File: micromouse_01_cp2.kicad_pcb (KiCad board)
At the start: 4 copper layers, 51.9 x 53 mm, 102 parts, among them IC1 ESP32-S3FH4R2, IC2 MPU-6500, IC3 AS5047P-ATSM, IC4 AS5047P-ATSM, IC5 DRV8835DSSR, IC6 PCA9632TK,118, J1 Conn_01x02, J2 USB_B_Micro, M1 MK06-4.5, M2 MK06-4.5, M3 Fan_Motor, Q1 MCM3400A-TP, Q2 MCM3400A-TP, Q3 MCM3400A-TP, Q4 SSM6J808R_LXHF, SW1 SSSS810701, SW2 SW_Push, U1 SMT-0440-S-R, U2 LBR-127HLD, U3 LBR-127HLD, U4 LBR-127HLD, U5 LBR-127HLD, U6 LXDC55FAAA-203, U7 RTV-104DF333-S-40.000-TR, U8 WS2812-2020

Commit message: エンコーダ基板シルク追加
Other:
- board text added: "L"
- board text added: "R"
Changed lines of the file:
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@@
   (gr_line (start 138 103.5) (end 132 104.000001)
     (stroke (width 0.2) (type solid)) (layer "Edge.Cuts"))
-  (gr_rect (start 118.115 79.938) (end 127.115 87.938)
+  (gr_rect locked (start 118.115 79.938) (end 127.115 87.938)
     (stroke (width 0.1) (type default)) (fill none) (layer "Edge.Cuts"))
   (gr_circle (center 162.5 102.25) (end 162.5 103.05)
@@
   (gr_circle (center 162.5 78.75) (end 162.5 79.55)
     (stroke (width 0.2) (type solid)) (fill none) (layer "Edge.Cuts"))
-  (gr_rect (start 118.68 93.26) (end 127.68 101.26)
+  (gr_rect locked (start 118.68 93.26) (end 127.68 101.26)
     (stroke (width 0.1) (type default)) (fill none) (layer "Edge.Cuts"))
+  (gr_text "L" (at 126.5 94.236191 90) (layer "B.SilkS")
+    (effects (font (size 5 5) (thickness 1) bold) (justify left bottom mirror))
+  )
+  (gr_text "R" (at 125.935 80.438 90) (layer "B.SilkS")
+    (effects (font (size 5 5) (thickness 1) bold) (justify left bottom mirror))
+  )
   (dimension (type aligned) (layer "Dwgs.User")
     (pts (xy 115.13 93.69) (xy 114.63 93.69))

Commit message: 仮変更
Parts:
- removed C12: 22u, Capacitor_SMD:C_0603_1608Metric
- removed C20, C22, C23: 1u, Capacitor_SMD:C_0402_1005Metric
- removed C21: 10u, Capacitor_SMD:C_0603_1608Metric
- removed C24: 0.01u, Capacitor_SMD:C_0402_1005Metric
- removed C25, C26, C27, C28, C29, C30, C31, C32, C35: 0.1u, Capacitor_SMD:C_0402_1005Metric
- removed IC1: ESP32-S3FH4R2, footprints:QFN40P700X700X90-57N-D
- removed J2: USB_B_Micro, footprints:WURTH_614105150721
- removed L1: 2.0nH, Inductor_SMD:L_0402_1005Metric
- removed R20: 47k, Resistor_SMD:R_0402_1005Metric
- removed SW1: SSSS810701, footprints:SSSS810701
- added C33: 0.1u, Capacitor_SMD:C_0402_1005Metric, F.Cu at (174.4, 87.0)
- added C34: 0.1u, Capacitor_SMD:C_0402_1005Metric, F.Cu at (174.4, 89.0)
- added C36: 0.1u, Capacitor_SMD:C_0402_1005Metric, F.Cu at (174.4, 91.0)
- added C37: 22u, Capacitor_SMD:C_0603_1608Metric, F.Cu at (184.6, 95.0)
- added C38: 0.1u, Capacitor_SMD:C_0402_1005Metric, F.Cu at (174.4, 92.9)
- added C41: 1u, Capacitor_SMD:C_0402_1005Metric, F.Cu at (174.4, 94.9)
- added C9: 0.1u, Capacitor_SMD:C_0402_1005Metric, F.Cu at (174.4, 85.1)
- added D7: CCS15S40,L3F, footprints:SOD-963 CST2C_TOS, F.Cu at (207.0, 115.5)
- added J3: ~, footprints:ZX62R-B-5P_30_, F.Cu at (144.3, 110.0)
- added J3: Conn_01x02_Pin, footprints:power_SMD, F.Cu at (152.5, 104.3)
- added Q5: Q_PMOS_GSD, Package_TO_SOT_SMD:SOT-23, F.Cu at (190.8, 107.1)
- added Q6: Q_PMOS_GSD, Package_TO_SOT_SMD:SOT-23, F.Cu at (190.8, 111.6)
- added R21: 10k, Resistor_SMD:R_0402_1005Metric, F.Cu at (184.1, 97.2)
- added R27: 47k, Resistor_SMD:R_0402_1005Metric, F.Cu at (194.7, 110.2)
- added R28: 47k, Resistor_SMD:R_0402_1005Metric, F.Cu at (194.7, 112.2)
- added R29: 470, Resistor_SMD:R_0402_1005Metric, F.Cu at (194.7, 114.1)
- added R32: 20, Resistor_SMD:R_0402_1005Metric, F.Cu at (209.7, 108.8)
- added R33: 20, Resistor_SMD:R_0402_1005Metric, F.Cu at (209.7, 110.8)
- added SW3: SSSS810701, footprints:SSSS810701, F.Cu at (136.3, 105.4)
- added U9: ESP32-S3-PICO-1-N8R2, footprints:QFN56_7X7_EXP, F.Cu at (151.0, 75.0)
- C18: value 0.1u -> 4.7u
- C19: value 1u -> 4.7u
- D4: value ESD9B3.3ST5G -> LED; footprint Diode_SMD:D_SOD-923 -> LED_SMD:LED_0402_1005Metric
- D5: value ESD9B3.3ST5G -> CCS15S40,L3F; footprint Diode_SMD:D_SOD-923 -> footprints:SOD-963 CST2C_TOS
- J1: value Conn_01x02 -> Conn_01x02_Pin; footprint Connector_JST:JST_PH_B2B-PH-K_1x02_P2.00mm_Vertical -> footprints:power_SMD
- Q4: value SSM6J808R_LXHF -> Q_PMOS_GSD; footprint footprints:TSOP6F_SSM6J_TOS -> Package_TO_SOT_SMD:SOT-23
- R24: value 10k -> 47k
- U7: value RTV-104DF333-S-40.000-TR -> MCP73831-2-OT; footprint Crystal:Crystal_SMD_2016-4Pin_2.0x1.6mm -> Package_TO_SOT_SMD:SOT-23-5
- moved C19 61.1 mm to (202.7, 110.1), turned to 0 degrees
- moved J1 60.8 mm to (203.7, 101.2)
- moved C18 56.8 mm to (202.7, 108.2), turned to 0 degrees
- moved R19 47.8 mm to (182.0, 71.0), turned to 0 degrees
- moved U1 47.3 mm to (168.4, 105.2)
- moved D1 46.9 mm to (167.3, 108.7), turned to 0 degrees
- moved C17 46.6 mm to (184.9, 74.7), turned to 0 degrees
- moved R18 45.5 mm to (190.8, 93.4), turned to 0 degrees
- moved U7 44.6 mm to (198.7, 109.4), turned to 0 degrees
- moved C11 43.6 mm to (184.9, 72.7), turned to 0 degrees
- moved M3 43.5 mm to (187.8, 72.5)
- moved D2 43.0 mm to (188.0, 76.2)
- moved R24 42.4 mm to (194.7, 108.2), turned to 0 degrees
- moved D5 41.7 mm to (207.0, 113.0), turned to 0 degrees
- moved Q4 41.3 mm to (190.3, 102.5), turned to 0 degrees
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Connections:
- C14 pad 1: Net-(J2-VBUS) -> VBUS
- C18 pad 1: +3V3 -> GND
- C18 pad 2: GND -> VBUS
- C19 pad 1: +3V3 -> GND
- C19 pad 2: GND -> Net-(J1-Pin_2)
- D4 pad 1: GND -> Net-(D4-K)
- D4 pad 2: USB_D- -> VBUS
- D5 pad 1: GND -> Net-(D5-K)
- D5 pad 2: USB_D+ -> VBUS
- J1 pad 1: Net-(J1-Pin_1) -> GND
- J1 pad 2: GND -> Net-(J1-Pin_2)
- Q4 pad 1: +BATT -> Net-(D5-K)
- Q4 pad 2: +BATT -> Net-(J1-Pin_2)
- R24 pad 1: Net-(IC1-CHIP_PU) -> Net-(D5-K)
- R24 pad 2: Net-(IC1-VDD3P3_1) -> GND
- U7 pad 1: unconnected-(U7-Vc-Pad1) -> /micromouse_01-2/STAT
- U7 pad 3: Net-(IC1-XTAL_P) -> Net-(J1-Pin_2)
- U7 pad 4: +3V3 -> VBUS
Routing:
- net +3V3: track 267.2 -> 48.1 mm, vias 24 -> 15
- net GND: track 101.8 -> 39.7 mm, vias 226 -> 101
- net LED_R: track 60.3 -> 0.02 mm, vias 2 -> 0
- net LED_FR: track 54.3 -> 0.00 mm, vias 2 -> 0
- net +BATT: track 53.6 -> 14.6 mm, vias 47 -> 6
- net SENS_L: track 39.3 -> 1.82 mm, vias 1 -> 0
- net LED_SDA: track 39.3 -> 2.25 mm, vias 2 -> 0
- net SENS_FR: track 43.5 -> 7.27 mm, vias 1 -> 0
- net LED_SCL: track 37.4 -> 1.31 mm, vias 2 -> 0
- net LED_FL: track 36.4 -> 1.31 mm, vias 2 -> 0
- net SENS_R: track 39.5 -> 4.99 mm, vias 1 -> 0
- net NeoPixel: track 34.3 -> 0.00 mm, vias 2 -> 0
- net USB_D-: track 33.2 -> 0.00 mm, vias 2 -> 0
- net SENS_FL: track 35.3 -> 3.36 mm, vias 1 -> 0
- net USB_D+: track 31.4 -> 0.00 mm, vias 2 -> 0
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- removed copper zone on B.Cu, net GND
- removed copper zone on In2.Cu, net GND
- removed copper zone on F.Cu, net Net-(D2-A)
- removed copper zone on F.Cu, net Net-(J1-Pin_1)
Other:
- board size 51.9 x 53 mm -> 53.9 x 53 mm

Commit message: [update]けっこう線引いた
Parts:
- removed D2: CCS15S40,L3F, footprints:SOD-963 CST2C_TOS
- removed the J3 at (152.5, 104.3)
- removed M3: Fan_Motor, footprints:MK06-4.5
- removed SW2: SW_Push, footprints:BOOT_PAD
- added J2: Fan+, footprints:Pad_1, F.Cu at (161.4, 93.2)
- added J4: Fan-, footprints:Pad_1, F.Cu at (161.9, 102.2)
- added REF**: Texas_SWRA117D_2.4GHz_Right, RF_Antenna:Texas_SWRA117D_2.4GHz_Right, F.Cu at (160.5, 80.2)
- J1: footprint footprints:power_SMD -> footprints:MK06-4.5
- R24, R27: value 47k -> R
- moved R32 71.4 mm to (138.6, 101.5)
- moved R33 70.0 mm to (140.5, 100.1)
- moved C19 65.8 mm to (140.5, 88.7), turned to 180 degrees
- moved D5 65.5 mm to (145.6, 90.0)
- moved C8 64.5 mm to (133.7, 69.9), turned to 180 degrees
- moved D7 64.3 mm to (147.9, 90.0), turned to 180 degrees
- moved C18 63.8 mm to (140.5, 94.0), turned to 180 degrees
- moved D4 61.9 mm to (142.2, 107.7), turned to 180 degrees
- moved U7 60.1 mm to (141.3, 91.4), turned to -90 degrees
- moved J1 58.5 mm to (147.3, 85.4), turned to 180 degrees
- moved R24 55.8 mm to (142.4, 88.7), turned to 180 degrees
- moved R3 55.4 mm to (149.5, 66.2), turned to -90 degrees
- moved R28 55.3 mm to (142.4, 94.0)
- moved R29 51.0 mm to (144.1, 107.7)
- moved R27 49.2 mm to (150.9, 87.6), turned to 90 degrees
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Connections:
- SW3 pad 1: GND -> Net-(Q6-G)
- SW3 pad 2: Net-(Q6-G) -> GND
- U9 pad 39: ENC_CLK -> ENC_MOSI
- U9 pad 41: ENC_MOSI -> ENC_CLK
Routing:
- net FAN_PWM: track 0.00 -> 52.1 mm, vias 0 -> 2
- net BUZZER: track 0.00 -> 39.5 mm, vias 0 -> 2
- net USB_D-: track 0.00 -> 33.6 mm
- net VBUS: track 0.00 -> 32.8 mm
- net VBATT: track 0.00 -> 31.4 mm, vias 0 -> 2
- net USB_D+: track 0.00 -> 30.9 mm
- net LED_FR: track 0.00 -> 25.1 mm, vias 0 -> 2
- net Net-(Q6-G): track 0.00 -> 23.6 mm
- net LED_R: track 0.02 -> 21.9 mm, vias 0 -> 2
- net IMU_MOSI: track 0.00 -> 19.8 mm, vias 0 -> 2
- net /micromouse_01-2/STAT: track 0.00 -> 18.9 mm, vias 0 -> 2
- net SENS_FR: track 7.27 -> 25.3 mm
- net GND: track 39.7 -> 22.6 mm, vias 101 -> 0
- net ENCL_CS: track 1.63 -> 18.1 mm, vias 1 -> 2
- net IMU_MISO: track 0.00 -> 16.4 mm, vias 0 -> 2
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- removed copper zone on F.Cu, net +3V3
- removed copper zone on In1.Cu, net +3V3
- removed copper zone on F.Cu, net +BATT
- removed copper zone on In1.Cu, net +BATT
- removed copper zone on F.Cu, net GND
- removed copper zone on In1.Cu, net GND
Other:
- board size 53.9 x 53 mm -> 69.3 x 51.4 mm

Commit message: とりあえず回路図完成
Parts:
- added C12: 1u, Capacitor_SMD:C_0402_1005Metric, F.Cu at (102.0, 79.0)
- added C20: 1u, Capacitor_SMD:C_0402_1005Metric, F.Cu at (102.0, 81.0)
- added U10: MA730, Package_DFN_QFN:QFN-16-1EP_3x3mm_P0.5mm_EP1.75x1.75mm, F.Cu at (97.9, 80.7)
- added U11: MA730, Package_DFN_QFN:QFN-16-1EP_3x3mm_P0.5mm_EP1.75x1.75mm, F.Cu at (97.9, 85.9)
- moved C33 23.9 mm to (150.8, 64.4), turned to 90 degrees
- moved C9 23.7 mm to (150.9, 66.3), turned to 90 degrees
- moved R15 22.3 mm to (157.6, 66.1)
- moved R8 19.9 mm to (143.7, 65.8)
- moved R9 18.3 mm to (133.3, 68.4), turned to -90 degrees
- moved R4 17.4 mm to (136.2, 65.1), turned to -90 degrees
- moved R6 10.0 mm to (148.3, 62.5)
- moved R21 5.87 mm to (156.1, 68.1), turned to 180 degrees
- moved C41 4.42 mm to (156.5, 66.7), turned to -90 degrees
- moved U9 3.81 mm to (151.0, 71.4)
- moved C37 3.71 mm to (156.7, 70.1), turned to -90 degrees
- moved R3 3.44 mm to (150.7, 63.0), turned to 0 degrees
- moved C38 3.41 mm to (155.5, 69.5), turned to -90 degrees
- moved C16 0.58 mm to (151.4, 83.0)
- moved IC5 0.57 mm to (150.9, 81.0)
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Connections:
- C33 pad 1: SENS_R -> SENS_FR
- C9 pad 1: SENS_FR -> SENS_R
- U9 pad 10: SENS_R -> SENS_FR
- U9 pad 9: SENS_FR -> SENS_R
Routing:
- net IMU_CS: track 15.3 -> 2.28 mm
- net GND: track 22.6 -> 32.1 mm, vias 0 -> 2
- net IMU_CLK: track 14.5 -> 5.80 mm
- net SENS_FL: track 6.59 -> 15.1 mm, vias 1 -> 2
- net IMU_MOSI: track 19.8 -> 11.4 mm
- net MOT_MODE: track 9.80 -> 16.9 mm
- net SENS_R: track 15.8 -> 10.4 mm
- net MOT1_PHASE: track 10.0 -> 15.0 mm
- net MOT1_ENBL: track 10.1 -> 14.9 mm
- net MOT2_PHASE: track 10.8 -> 15.5 mm
- net MOT2_ENBL: track 10.4 -> 15.0 mm
- net ENC_CLK: track 21.2 -> 25.4 mm
- net ENC_MOSI: track 21.0 -> 25.1 mm
- net NeoPixel: track 13.2 -> 17.3 mm
- net ENC_MISO: track 20.8 -> 24.8 mm
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
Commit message: パターン配線中
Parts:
- removed C33, C34, C36: 0.1u, Capacitor_SMD:C_0402_1005Metric
- removed IC3, IC4: AS5047P-ATSM, footprints:SOP65P640X120-14N
- removed the REF** at (160.5, 80.2)
- added AE1: Antenna_Shield, RF_Antenna:Texas_SWRA117D_2.4GHz_Right, F.Cu at (160.7, 80.8)
- added C21: 0.1u, Capacitor_SMD:C_0402_1005Metric, F.Cu at (151.8, 58.3)
- added C22: 0.1u, Capacitor_SMD:C_0402_1005Metric, F.Cu at (150.0, 58.3)
- added C23: 0.1u, Capacitor_SMD:C_0402_1005Metric, F.Cu at (147.0, 58.2)
- added C24: 0.1u, Capacitor_SMD:C_0402_1005Metric, F.Cu at (147.6, 59.6)
- added C25: 3.3p, Capacitor_SMD:C_0402_1005Metric, F.Cu at (160.8, 73.2)
- added L1: 2.2n, Inductor_SMD:L_0402_1005Metric, F.Cu at (160.3, 74.6)
- added R20: 0, Resistor_SMD:R_0402_1005Metric, F.Cu at (154.5, 59.8)
- added U13: MCP3464T-E/NC, footprints:UQFN20_NC_MCH, F.Cu at (151.0, 60.9)
- C9: value 0.1u -> 3.3p
- moved U10 74.1 mm to (171.6, 88.7), turned to 90 degrees
- moved C12 67.7 mm to (169.0, 88.5), turned to -90 degrees
- moved REF** 63.6 mm to (174.5, 88.7)
- moved C7 59.3 mm to (153.6, 61.6), turned to -90 degrees
- moved R2 55.6 mm to (162.2, 97.3), turned to 90 degrees
- moved R1 54.8 mm to (162.2, 95.5), turned to -90 degrees
- moved C6 54.0 mm to (153.6, 59.9)
- moved C13 51.9 mm to (160.8, 94.0), turned to 180 degrees
- moved U11 32.5 mm to (130.4, 87.7), turned to 90 degrees
- moved C17 31.8 mm to (148.4, 61.4), turned to -90 degrees
- moved C20 26.6 mm to (127.8, 87.4), turned to -90 degrees
- moved REF** 23.3 mm to (133.4, 87.7)
- moved IC6 16.6 mm to (159.6, 96.3), turned to 0 degrees
- moved C4 14.6 mm to (140.3, 72.1), turned to -90 degrees
- moved IC2 14.5 mm to (142.9, 71.2)
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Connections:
- C9 pad 1: SENS_R -> Net-(AE1-A)
- U9 pad 1: unconnected-(U9-LNA_IN-Pad1) -> Net-(U9-LNA_IN)
- U9 pad 10: SENS_FR -> ADC_CS
- U9 pad 11: ENCL_CS -> unconnected-(U9-GPIO6-Pad11)
- U9 pad 12: IMU_CS -> unconnected-(U9-GPIO7-Pad12)
- U9 pad 13: SENS_L -> ENCL_CS
- U9 pad 15: SENS_FL -> LED_L
- U9 pad 16: IMU_MISO -> FAN_PWM
- U9 pad 17: IMU_MOSI -> unconnected-(U9-GPIO12-Pad17)
- U9 pad 18: FAN_PWM -> BUZZER
- U9 pad 19: BUZZER -> IMU_CS
- U9 pad 24: LED_L -> unconnected-(U9-GPIO18-Pad24)
- U9 pad 42: LED_SDA -> LED_SCL
- U9 pad 43: LED_SCL -> LED_SDA
- U9 pad 7: IMU_CLK -> IMU_MISO
- U9 pad 8: VBATT -> IMU_MOSI
- U9 pad 9: SENS_R -> IMU_CLK
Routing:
- net GND: track 32.1 -> 81.9 mm, vias 2 -> 26
- net +3V3: track 44.9 -> 80.5 mm, vias 0 -> 10
- net LED_SCL: track 0.00 -> 34.4 mm, vias 0 -> 2
- net LED_SDA: track 0.00 -> 33.8 mm, vias 0 -> 2
- net VBATT: track 35.2 -> 63.1 mm
- net Net-(D3-K): track 0.00 -> 18.0 mm, vias 0 -> 2
- net Net-(D8-K): track 0.00 -> 15.4 mm, vias 0 -> 2
- net Net-(D9-K): track 0.00 -> 12.6 mm, vias 0 -> 2
- net ENC_MOSI: track 25.1 -> 36.9 mm, vias 2 -> 4
- net ENCL_CS: track 18.0 -> 29.6 mm, vias 2 -> 3
- net SENS_FL: track 15.1 -> 26.6 mm, vias 2 -> 1
- net ENCR_CS: track 13.3 -> 24.5 mm, vias 2 -> 3
- net Net-(U9-LNA_IN): track 0.00 -> 11.2 mm
- net Net-(D10-K): track 0.00 -> 9.50 mm, vias 0 -> 2
- net ENC_CLK: track 25.4 -> 34.8 mm, vias 2 -> 4
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- added copper zone on F.Cu, net +BATT
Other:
- board size 69.3 x 51.4 mm -> 51.2 x 51.4 mm
- board text removed: "L"
- board text removed: "R"

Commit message: アンテナ除去中
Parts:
- moved R32 1.25 mm to (139.8, 101.5)
- moved C15 0.85 mm to (151.1, 85.1)
- moved R5 0.61 mm to (140.8, 63.4)
- moved R31 0.52 mm to (153.4, 106.8)
- moved R25 0.52 mm to (148.6, 106.8)
- moved C14 0.47 mm to (140.9, 103.0)
- moved R33 0.45 mm to (140.5, 100.5)
- moved U1 0.45 mm to (168.6, 105.1)
- moved R17 0.43 mm to (159.2, 99.8)
- moved Q3 0.40 mm to (161.3, 100.3)
- moved D4 0.40 mm to (142.2, 107.3)
- moved R29 0.40 mm to (144.1, 107.3)
- moved D6 0.39 mm to (155.6, 107.3)
- moved R16 0.39 mm to (157.4, 107.3)
- moved R30 0.25 mm to (151.5, 106.8)
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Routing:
- net GND: track 81.9 -> 101.1 mm, vias 26 -> 53
- net +3V3: track 80.5 -> 70.7 mm, vias 10 -> 18
- net BUZZER: track 44.0 -> 41.6 mm
- net MOT_MODE: track 17.7 -> 16.1 mm
- net LED_SCL: track 34.4 -> 35.9 mm
- net LED_SDA: track 33.8 -> 35.0 mm
- net Net-(J3-D-): track 3.03 -> 4.16 mm
- net ENC_CLK: track 34.8 -> 35.9 mm
- net MOT2_ENBL: track 15.8 -> 16.9 mm
- net VBUS: track 32.8 -> 33.8 mm
- net SENS_R: track 17.2 -> 18.0 mm
- net MOT1_ENBL: track 15.6 -> 16.3 mm
- net MOT2_PHASE: track 16.3 -> 17.0 mm
- net USB_D-: track 37.2 -> 36.4 mm
- net MOT1_PHASE: track 15.7 -> 16.4 mm
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- added copper zone on F.Cu, net +3V3
- added copper zone on In1.Cu, net +3V3
- added copper zone on B.Cu, net GND
- added copper zone on F.Cu, net GND
- added copper zone on In2.Cu, net GND
- added copper zone on F.Cu, net Net-(J1-Pin_2)

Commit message: [add]3Dモデル追加
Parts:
- moved R2 12.5 mm to (151.7, 90.7), turned to 0 degrees
- moved R1 12.0 mm to (151.7, 89.7), turned to 0 degrees
- moved C23 2.43 mm to (149.4, 58.3), turned to 90 degrees
- moved C6 1.97 mm to (153.8, 61.9), turned to -90 degrees
- moved C7 1.76 mm to (154.8, 60.3), turned to 90 degrees
- moved C11 1.39 mm to (156.1, 93.3), turned to 0 degrees
- moved J2 1.34 mm to (154.3, 91.7), turned to 180 degrees
- moved IC6 1.10 mm to (160.7, 96.3)
- moved R27 0.90 mm to (150.6, 86.8)
- moved C24 0.90 mm to (148.4, 59.6)
- moved R18 0.89 mm to (155.5, 91.9), turned to 90 degrees
- moved R6 0.87 mm to (147.4, 59.6)
- moved C13 0.83 mm to (161.7, 94.0), turned to 0 degrees
- moved R19 0.81 mm to (156.5, 91.9)
- moved R20 0.74 mm to (153.8, 59.9)
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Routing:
- net +3V3: track 70.7 -> 259.7 mm, vias 18 -> 35
- net GND: track 101.1 -> 82.3 mm, vias 53 -> 47
- net Net-(D10-K): track 9.59 -> 13.3 mm
- net VBATT: track 63.1 -> 59.6 mm
- net IMU_MISO: track 24.3 -> 21.9 mm
- net SENS_R: track 18.0 -> 20.3 mm
- net Net-(D3-K): track 17.9 -> 19.9 mm
- net LED_SCL: track 35.9 -> 34.4 mm, vias 2 -> 3
- net Net-(R11-Pad1): track 4.28 -> 5.72 mm
- net Net-(D8-K): track 15.4 -> 16.9 mm
- net Net-(D9-K): track 12.6 -> 13.9 mm
- net +BATT: track 18.7 -> 17.5 mm
- net Net-(U13-REFIN+): track 3.85 -> 2.76 mm
- net LED_SDA: track 35.0 -> 33.9 mm, vias 2 -> 3
- net IMU_CLK: track 14.7 -> 13.8 mm
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- removed copper zone on In1.Cu, net +3V3
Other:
- outline, holes or cut-outs redrawn

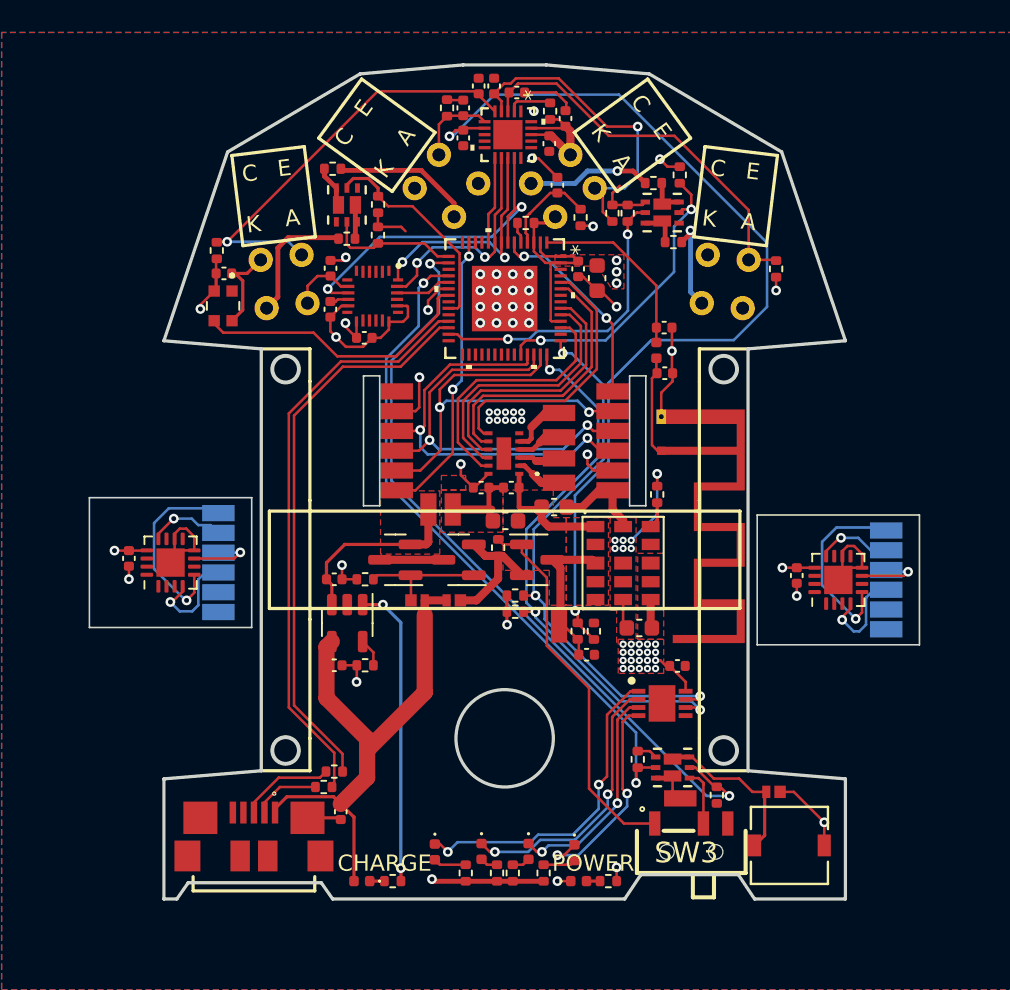
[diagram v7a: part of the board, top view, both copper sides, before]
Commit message: アンテナ除去した
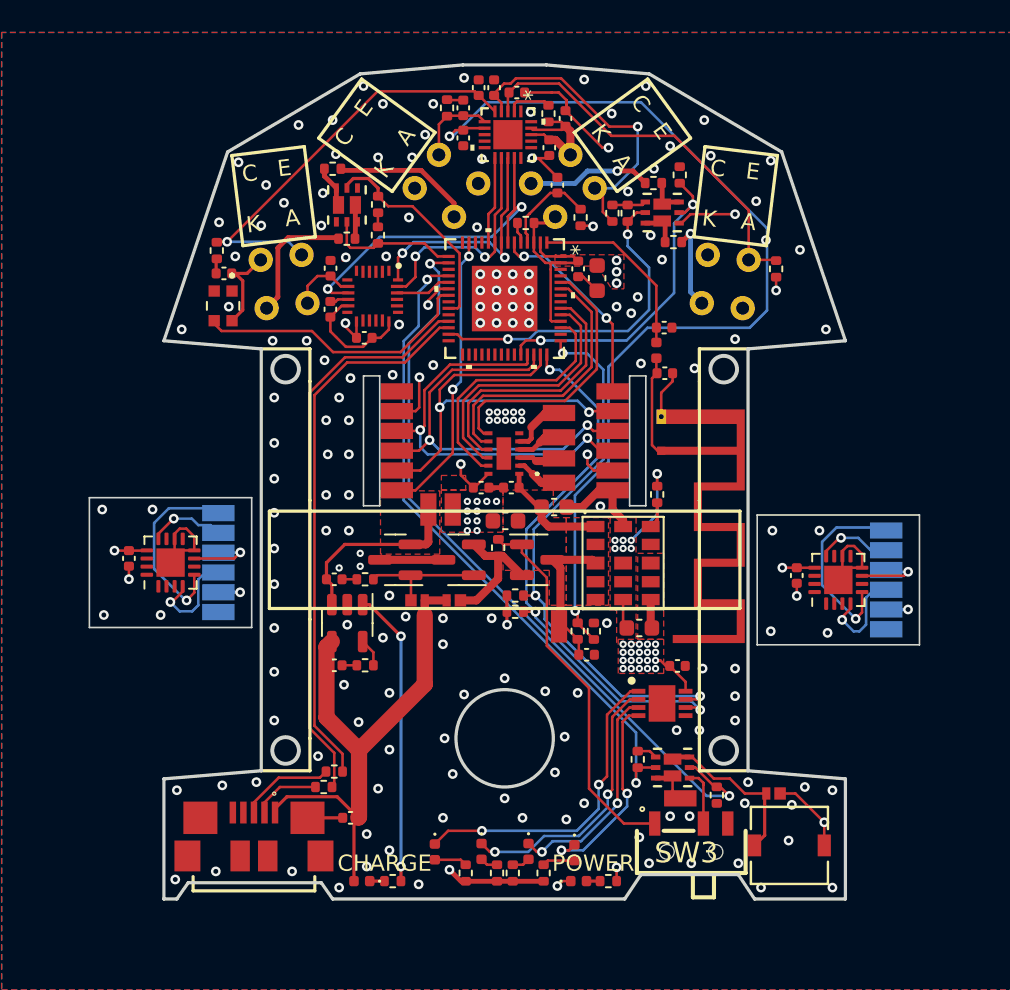
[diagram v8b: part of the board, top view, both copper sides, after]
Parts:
- moved C14 0.71 mm to (141.5, 103.4), turned to 180 degrees
- moved C6 0.25 mm to (153.8, 62.1)
- moved R20 0.18 mm to (153.7, 60.0)
- moved D1 0.10 mm to (167.6, 101.9)
- moved C22 0.10 mm to (150.3, 58.4)
- moved C23 0.10 mm to (149.4, 58.4)
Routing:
- net GND: track 82.3 -> 71.0 mm, vias 47 -> 191
- net +3V3: track 259.7 -> 266.4 mm, vias 35 -> 37
- net LED_R: track 18.7 -> 20.5 mm
- net LED_FR: track 18.9 -> 20.0 mm
- net USB_D-: track 36.4 -> 35.4 mm
- net USB_D+: track 34.9 -> 33.9 mm
- net VBATT: track 59.6 -> 60.5 mm, vias 2 -> 3
- net BUZZER: track 42.0 -> 41.1 mm
- net FAN_PWM: track 48.1 -> 47.2 mm
- net Net-(D10-K): track 13.3 -> 12.6 mm
- net +BATT: track 17.5 -> 16.8 mm
- net LED_SDA: track 33.9 -> 34.4 mm
- net VBUS: track 33.8 -> 34.3 mm
- added copper zone on In1.Cu, net +3V3
- added copper zone on In1.Cu, net GND
